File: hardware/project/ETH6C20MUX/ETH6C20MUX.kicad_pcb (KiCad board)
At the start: 4 copper layers, 160 x 100 mm, 184 parts, among them J301 5499141-4, J501 Conn_01x06, J502 Conn_02x08_Odd_Even, J503 C64AC, J601 Conn_02x05, J602 Conn_02x01, K301 HE3621A0510, K302 HE3621A0510, K303 HE3621A0510, K304 HE3621A0510, K305 HE3621A0510, K306 HE3621A0510, K307 HE3621A0510, K308 HE3621A0510, K309 HE3621A0510, K310 HE3621A0510, K311 HE3621A0510, K312 HE3621A0510, K313 HE3621A0510, K314 HE3621A0510, K315 HE3621A0510, K316 HE3621A0510, K317 HE3621A0510, K318 HE3621A0510, K319 HE3621A0510, K320 HE3621A0510, K321 HE3621A0510, K322 HE3621A0510, K323 HE3621A0510, K324 HE3621A0510, K325 HE3621A0510, K326 HE3621A0510, K327 HE3621A0510, K328 HE3621A0510, K329 HE3621A0510, K330 HE3621A0510, K331 HE3621A0510, K332 HE3621A0510, K333 HE3621A0510, K334 HE3621A0510, K335 HE3621A0510, K336 HE3621A0510, K337 HE3621A0510, K338 HE3621A0510, K339 HE3621A0510, K340 HE3621A0510, K341 HE3621A0510, K342 HE3621A0510, K343 HE3621A0510, K344 HE3621A0510, K345 HE3621A0510, K346 HE3621A0510, K347 HE3621A0510, K348 HE3621A0510, K349 HE3621A0510, K350 HE3621A0510, K351 HE3621A0510, K352 HE3621A0510, K353 HE3621A0510, K354 HE3621A0510, K355 HE3621A0510, K356 HE3621A0510, K357 HE3621A0510, K358 HE3621A0510, K359 HE3621A0510, K360 HE3621A0510, K361 HE3621A0510, K362 HE3621A0510, K363 HE3621A0510, K364 HE3621A0510, K365 HE3621A0510, K366 HE3621A0510, Q401 IRFR5410, U201 LC03-3.3, U202 LAN8742A, U203 LC03-3.3, U301 MCZ33996, U302 MCZ33996, U303 MCZ33996, U304 MCZ33996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

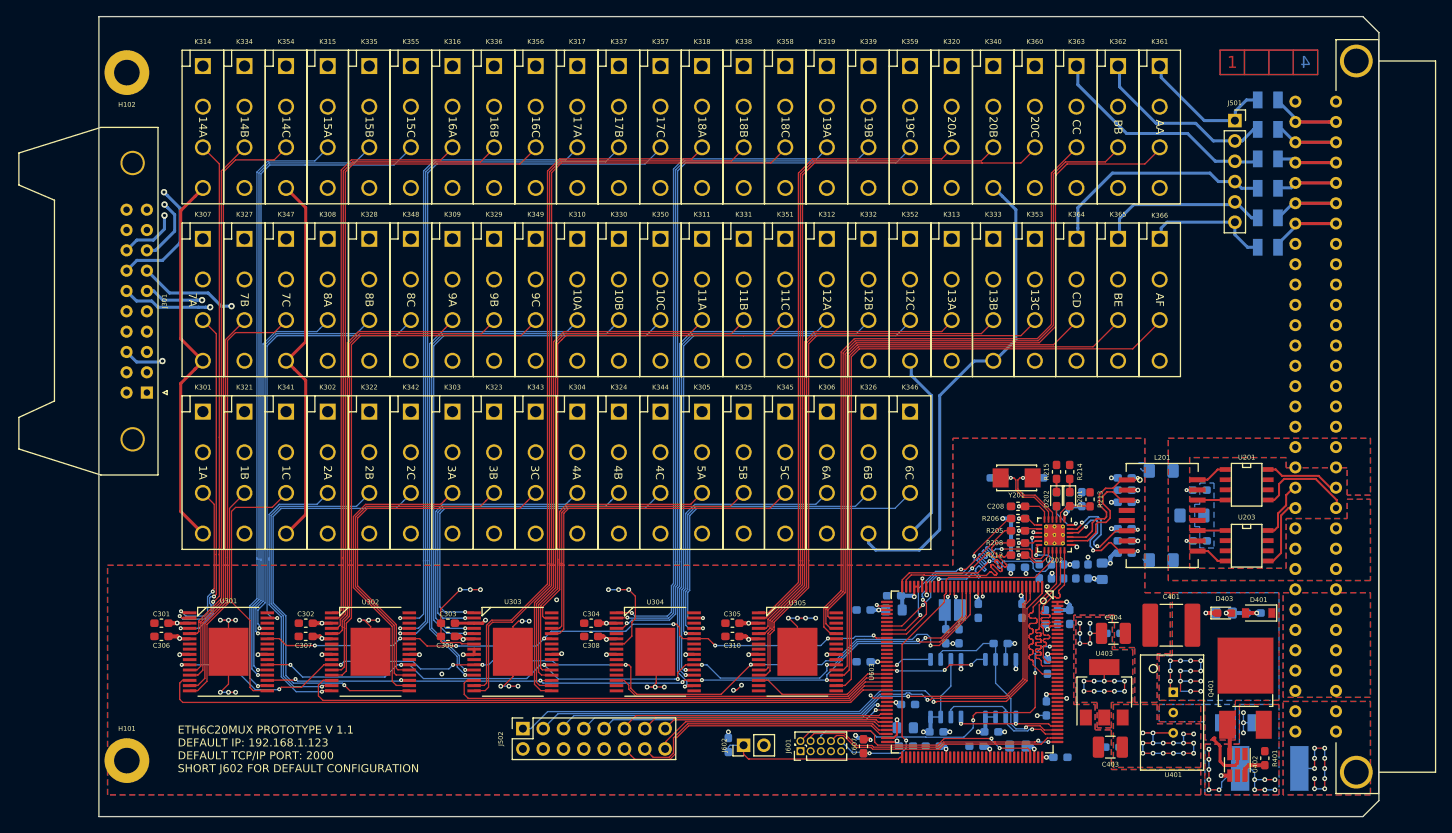
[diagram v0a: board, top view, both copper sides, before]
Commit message: Added pin swap for A,B,E and F.
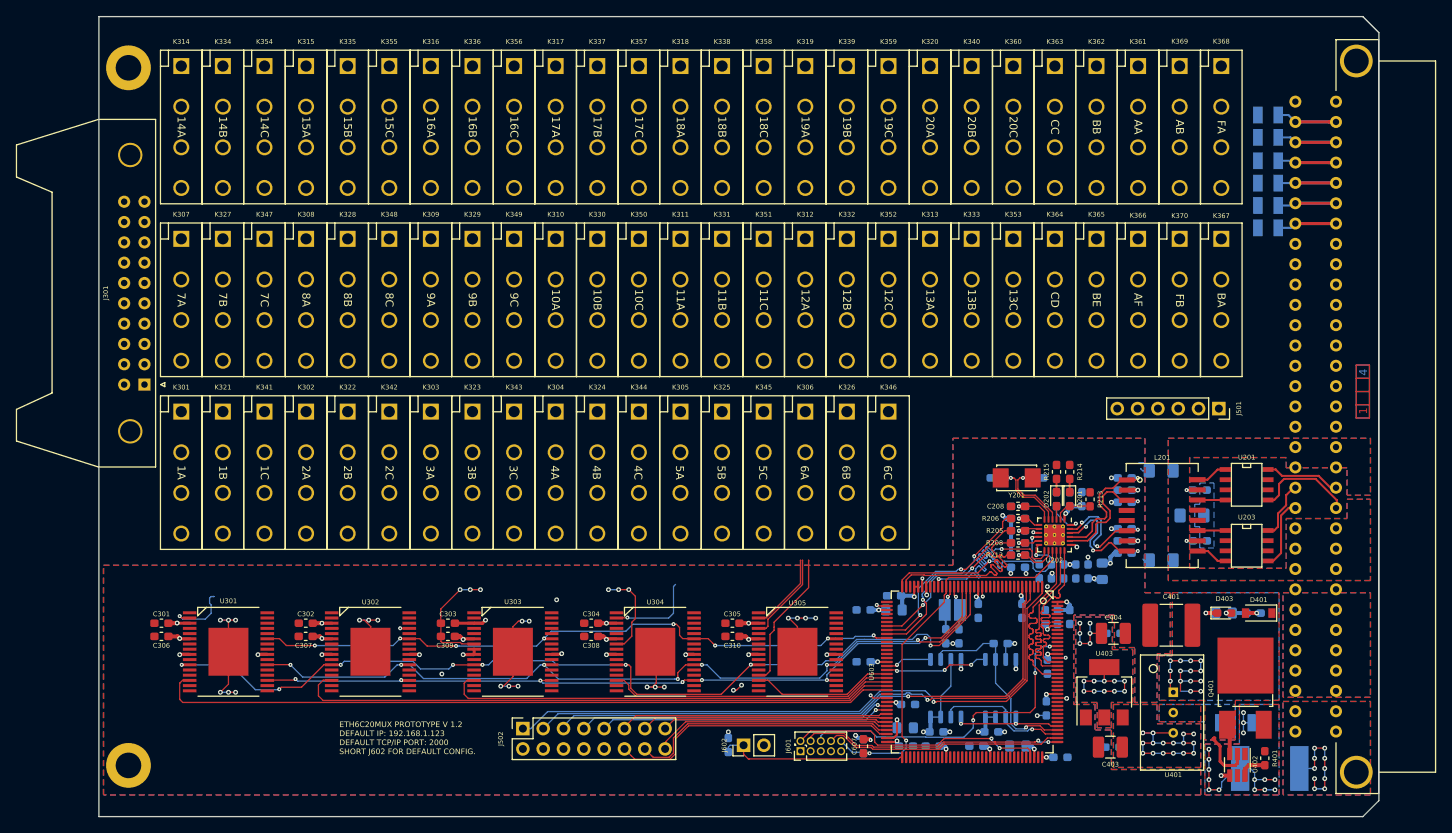
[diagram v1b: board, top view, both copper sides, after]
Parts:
- added K367: HE3621A0510, ETH6C20MUX:HE360_x-5050462-8, F.Cu at (200.3, 75.4)
- added K368: HE3621A0510, ETH6C20MUX:HE360_x-5050462-8, F.Cu at (200.3, 53.8)
- added K369: HE3621A0510, ETH6C20MUX:HE360_x-5050462-8, F.Cu at (195.1, 53.8)
- added K370: HE3621A0510, ETH6C20MUX:HE360_x-5050462-8, F.Cu at (195.1, 75.4)
- U601, U602: value S25FL064L_SOIC -> S25FL064L
- moved J501 36.1 mm to (200.0, 89.0), turned to 270 degrees
- moved K305 2.70 mm to (132.7, 97.0)
- moved K311 2.70 mm to (132.7, 75.4)
- moved K318 2.70 mm to (132.7, 53.8)
- moved K333 2.70 mm to (169.1, 75.4)
- moved K340 2.70 mm to (169.1, 53.8)
- moved K345 2.70 mm to (143.1, 97.0)
- moved K346 2.70 mm to (158.7, 97.0)
- moved K351 2.70 mm to (143.1, 75.4)
- moved K352 2.70 mm to (158.7, 75.4)
- moved K358 2.70 mm to (143.1, 53.8)
- moved K359 2.70 mm to (158.7, 53.8)
- moved K362 2.70 mm to (184.7, 53.8)
- moved K365 2.70 mm to (184.7, 75.4)
- moved K301 2.70 mm to (70.3, 97.0)
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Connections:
- U305 pad 15: (no net) -> /Relays/RELAYBA
- U305 pad 16: (no net) -> /Relays/RELAYEA
- U305 pad 17: (no net) -> /Relays/RELAYAB
- U305 pad 32: (no net) -> /Relays/RELAYFA
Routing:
- net /Relays/PIN10C: track 449.6 -> 0.00 mm
- net /Relays/PIN10B: track 435.5 -> 0.00 mm
- net /Relays/PIN10A: track 428.7 -> 0.00 mm
- net /Relays/PIN20: track 131.4 -> 0.00 mm
- net /Relays/PIN13: track 118.7 -> 0.00 mm, vias 1 -> 0
- net /Relays/PIN19: track 113.6 -> 0.00 mm
- net /Relays/PIN12: track 104.6 -> 0.00 mm, vias 1 -> 0
- net /Relays/PIN18: track 101.4 -> 0.00 mm
- net /Relays/PIN6: track 101.3 -> 0.00 mm, vias 1 -> 0
- net /Relays/RELAY18C: track 98.1 -> 0.00 mm
- net /Relays/RELAY18B: track 96.7 -> 0.00 mm
- net /Relays/RELAYA: track 96.0 -> 0.00 mm
- net /Relays/RELAY19C: track 94.1 -> 0.00 mm, vias 1 -> 0
- net /Relays/RELAYB: track 93.2 -> 0.66 mm
- net /Relays/RELAY17C: track 92.0 -> 0.00 mm, vias 1 -> 0
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- added copper zone on Power, net Earth
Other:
- board text added: "AB"
- board text added: "BA"
- board text added: "ETH6C20MUX PROTOTYPE V 1.2 DEFAULT IP: 192.168.1.123 DEFAULT TCP/IP PORT: 2000 SHORT J602 FOR DEFAULT CONFIG."
- board text added: "FA"
- board text added: "FB"
- board text removed: "ETH6C20MUX PROTOTYPE V 1.1 DEFAULT IP: 192.168.1.123 DEFAULT TCP/IP PORT: 2000 SHORT J602 FOR DEFAULT CONFIGURATION"

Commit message: PCB redesign
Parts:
- added D601: RED, LED_SMD:LED_0603_1608Metric_Pad1.05x0.95mm_HandSolder, F.Cu at (63.5, 113.7)
- added D602: GREEN, LED_SMD:LED_0603_1608Metric_Pad1.05x0.95mm_HandSolder, F.Cu at (63.5, 116.7)
- added D603: BLUE, LED_SMD:LED_0603_1608Metric_Pad1.05x0.95mm_HandSolder, F.Cu at (63.5, 119.5)
- added H103: MountingHole, MountingHole:MountingHole_2.7mm_M2.5_DIN965_Pad, F.Cu at (211.0, 46.0)
- added R602: 680, Resistor_SMD:R_0603_1608Metric_Pad0.98x0.95mm_HandSolder, F.Cu at (67.2, 113.7)
- added R603: 680, Resistor_SMD:R_0603_1608Metric_Pad0.98x0.95mm_HandSolder, F.Cu at (67.2, 116.7)
- added R605: 680, Resistor_SMD:R_0603_1608Metric_Pad0.98x0.95mm_HandSolder, F.Cu at (67.2, 119.5)
- added RN601: 10k, Resistor_SMD:R_Array_Convex_5x0603, B.Cu at (99.6, 131.3)
- added SW601: A6SN-5104, Button_Switch_SMD:SW_DIP_SPSTx05_Slide_6.7x14.26mm_W8.61mm_P2.54mm_LowProfile, F.Cu at (99.6, 131.3)
- C201, C202, C203, C204, C205, C206, C207, C208, C209, C210, C213, C214, C402, C405, C601, C602, C603, C604, C607, C608, C609, C610, C611, C612, C613, C614, C615, C616, C617, C618, C619, C620, C621: footprint Capacitor_SMD:C_0603_1608Metric_Pad1.05x0.95mm_HandSolder -> Capacitor_SMD:C_0603_1608Metric_Pad1.08x0.95mm_HandSolder
- C301, C302, C303, C304, C305, C306, C307, C308, C309, C310: footprint Capacitor_SMD:C_0603_1608Metric_Pad1.05x0.95mm_HandSolder -> Capacitor_SMD:C_0603_1608Metric_Pad1.08x0.95mm_HandSolder; moved to B.Cu
- D201: value YELLOW -> GREEN
- D202: value GREEN -> YELLOW
- H101, H102: footprint MountingHole:MountingHole_3.2mm_M3_DIN965_Pad -> MountingHole:MountingHole_2.7mm_M2.5_DIN965_Pad
- R201, R202, R203, R204, R205, R206, R207, R208, R209, R210, R211, R212, R213, R214, R215, R217, R218, R219, R220, R221, R401, R403, R601, R604, R608, R609: footprint Resistor_SMD:R_0603_1608Metric_Pad1.05x0.95mm_HandSolder -> Resistor_SMD:R_0603_1608Metric_Pad0.98x0.95mm_HandSolder
- R216: footprint Resistor_SMD:R_1206_3216Metric_Pad1.42x1.75mm_HandSolder -> Resistor_SMD:R_0603_1608Metric_Pad0.98x0.95mm_HandSolder
- R402: footprint Resistor_SMD:R_0805_2012Metric_Pad1.15x1.40mm_HandSolder -> Resistor_SMD:R_0603_1608Metric_Pad0.98x0.95mm_HandSolder
- moved K360 93.6 mm to (80.7, 53.8)
- moved K320 93.6 mm to (70.3, 53.8)
- moved K340 93.6 mm to (75.5, 53.8)
- moved K334 93.5 mm to (169.0, 53.8)
- moved K314 93.5 mm to (163.8, 53.8)
- moved K354 93.5 mm to (174.2, 53.8)
- moved K319 62.4 mm to (85.9, 53.8)
- moved K339 62.4 mm to (91.1, 53.8)
- moved K359 62.4 mm to (96.3, 53.8)
- moved K355 62.4 mm to (158.7, 53.8)
- moved K315 62.4 mm to (148.3, 53.8)
- moved K335 62.4 mm to (153.5, 53.8)
- moved K338 31.2 mm to (106.7, 53.8)
- moved K318 31.2 mm to (101.5, 53.8)
- moved K358 31.2 mm to (111.9, 53.8)
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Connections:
- J501 pad 4: /Connector/D -> /Connector/F
- J501 pad 6: /Connector/F -> /Connector/D
- U301 pad 12: /Relays/RELAY14C -> /Relays/RELAY7B
- U301 pad 13: /Relays/RELAY7B -> /Relays/RELAY1B
- U301 pad 15: /Relays/RELAY7C -> /Relays/RELAY14C
- U301 pad 16: /Relays/RELAY1B -> /Relays/RELAY8C
- U301 pad 17: /Relays/RELAY1C -> /Relays/RELAY8B
- U301 pad 29: /Relays/RELAY8B -> (no net)
- U301 pad 31: /Relays/RELAY8C -> /Relays/RELAY7C
- U301 pad 32: (no net) -> /Relays/RELAY1C
- U301 pad 4: /Relays/RELAY14A -> /Relays/RELAY20A
- U301 pad 5: /Relays/RELAY14B -> /Relays/RELAY20B
- U305 pad 1: /Relays/RELAY20A -> /Relays/RELAY14A
- U305 pad 2: /Relays/RELAY20B -> /Relays/RELAY14B
- U603 pad 74: (no net) -> /MCU/ETH_CODE4
- U603 pad 75: (no net) -> /MCU/ETH_CODE3
- U603 pad 76: (no net) -> /MCU/ETH_CODE2
- U603 pad 77: (no net) -> /MCU/ETH_CODE1
- U603 pad 78: (no net) -> /MCU/ETH_CODE0
- U603 pad 80: (no net) -> Net-(R602-Pad2)
- U603 pad 81: (no net) -> Net-(R603-Pad2)
- U603 pad 82: (no net) -> Net-(R605-Pad2)
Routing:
- net /Relays/PIN10B: track 0.00 -> 446.1 mm
- net /Relays/PIN10A: track 0.00 -> 445.9 mm
- net /Relays/PIN10C: track 0.00 -> 366.8 mm
- net /Relays/PIN14: track 0.00 -> 132.0 mm
- net /Connector/C: track 0.00 -> 117.3 mm
- net /MCU/RELAY1_SCLK: track 118.0 -> 0.77 mm, vias 8 -> 0
- net /Relays/PIN13: track 0.00 -> 114.3 mm
- net Net-(R602-Pad2): track 0.00 -> 112.7 mm
- net Net-(R603-Pad2): track 0.00 -> 110.6 mm
- net /Relays/PIN15: track 0.00 -> 110.0 mm
- net Net-(R605-Pad2): track 0.00 -> 108.8 mm
- net /Relays/PIN6: track 0.00 -> 102.6 mm
- net /Relays/PIN12: track 0.00 -> 102.2 mm
- net /MCU/RELAY1_SO: track 103.7 -> 2.10 mm, vias 7 -> 1
- net /MCU/RELAY1_SI: track 98.6 -> 0.00 mm, vias 7 -> 0
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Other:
- net class Relay signal 100V: trace_width 0.381 -> 0.254
- board text added: "EA"
- board text removed: "FA"

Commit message: PCB design
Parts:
- D601, D602, D603: footprint LED_SMD:LED_0603_1608Metric_Pad1.05x0.95mm_HandSolder -> LED_SMD:LED_Dialight_591
- J501: value Conn_01x06 -> Conn_02x06_Odd_Even; footprint Connector_PinSocket_2.54mm:PinSocket_1x06_P2.54mm_Vertical -> Connector_PinSocket_2.54mm:PinSocket_2x06_P2.54mm_Vertical
- R216: footprint Resistor_SMD:R_0603_1608Metric_Pad0.98x0.95mm_HandSolder -> Resistor_SMD:R_1206_3216Metric_Pad1.30x1.75mm_HandSolder
- moved J501 11.2 mm to (189.0, 91.0)
- moved R605 6.16 mm to (68.7, 125.5)
- moved D603 5.98 mm to (63.1, 125.5)
- moved R603 3.41 mm to (68.7, 119.8)
- moved D602 3.07 mm to (63.1, 119.8)
- moved R602 1.57 mm to (68.7, 114.0)
- moved C212 1.09 mm to (192.4, 109.0)
- moved D601 0.54 mm to (63.1, 114.0)
- moved R216 0.54 mm to (192.4, 96.4)
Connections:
- J501 pad 2: /Connector/B -> /Connector/A
- J501 pad 3: /Connector/C -> /Connector/B
- J501 pad 4: /Connector/F -> /Connector/B
- J501 pad 5: /Connector/E -> /Connector/C
- J501 pad 6: /Connector/D -> /Connector/C
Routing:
- net /Connector/C: track 117.3 -> 35.0 mm
- net /Connector/A: track 75.7 -> 25.0 mm
- net /Connector/D: track 58.6 -> 32.4 mm
- net /Connector/B: track 72.1 -> 46.3 mm
- net /Connector/F: track 39.8 -> 16.1 mm
- net /Connector/E: track 66.3 -> 43.0 mm
- net +3V3: track 150.2 -> 128.8 mm, vias 44 -> 43
- net GND: track 42.4 -> 32.3 mm, vias 31 -> 28
- net Net-(R605-Pad2): track 108.8 -> 102.5 mm
- net Net-(R603-Pad2): track 110.6 -> 106.2 mm
- net Net-(R602-Pad2): track 112.7 -> 110.8 mm
- net Net-(D603-Pad1): track 1.90 -> 3.08 mm
- net Net-(D602-Pad1): track 1.90 -> 3.08 mm
- net Net-(D601-Pad1): track 1.90 -> 3.08 mm
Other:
- board text added: "ETH6C20MUX PROTOTYPE V 1.1 DEFAULT IP: 192.168.1.120 DEFAULT TCP/IP PORT: 2000 SHORT J602 FOR DEFAULT CONFIG."
- board text removed: "ETH6C20MUX PROTOTYPE V 1.2 DEFAULT IP: 192.168.1.123 DEFAULT TCP/IP PORT: 2000 SHORT J602 FOR DEFAULT CONFIG."

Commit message: PCB layout
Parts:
- moved C301 1.69 mm to (73.2, 113.4)
- moved U305 1.67 mm to (147.0, 117.0)
- moved C302 1.67 mm to (89.7, 113.4)
- moved C303 1.66 mm to (106.2, 113.4)
- moved C304 1.65 mm to (122.7, 113.4)
- moved C305 1.65 mm to (139.2, 113.4)
- moved U304 1.65 mm to (130.5, 117.0)
- moved U303 1.65 mm to (114.0, 117.0)
- moved U301 1.64 mm to (81.0, 117.0)
- moved U302 1.64 mm to (97.5, 117.0)
- moved C308 1.52 mm to (122.7, 115.4)
- moved C306 1.33 mm to (73.2, 115.4)
- moved C307 1.30 mm to (89.7, 115.4)
- moved C309 1.28 mm to (106.2, 115.4)
- moved C310 1.27 mm to (139.2, 115.4)
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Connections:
- K315 pad 3: /Relays/RELAY15A -> (no net)
- K335 pad 3: /Relays/RELAY15B -> (no net)
- K354 pad 3: /Relays/RELAY14C -> (no net)
- K355 pad 3: /Relays/RELAY15C -> (no net)
- U301 pad 1: /Relays/RELAY1A -> /Relays/RELAY20C
- U301 pad 12: /Relays/RELAY7B -> /Relays/RELAY20B
- U301 pad 13: /Relays/RELAY1B -> /Relays/RELAY20A
- U301 pad 15: /Relays/RELAY14C -> /Relays/RELAY7A
- U301 pad 16: /Relays/RELAY8C -> /Relays/RELAY1A
- U301 pad 17: /Relays/RELAY8B -> /Relays/RELAY1C
- U301 pad 18: /Relays/RELAY15A -> /Relays/RELAY19A
- U301 pad 2: /Relays/RELAY7A -> /Relays/RELAY7C
- U301 pad 20: /Relays/RELAY15B -> /Relays/RELAY8A
- U301 pad 21: /Relays/RELAY15C -> /Relays/RELAY2A
- U301 pad 28: /Relays/RELAY8A -> (no net)
- U301 pad 29: (no net) -> /Relays/RELAY2B
- U301 pad 31: /Relays/RELAY7C -> /Relays/RELAY8B
- U301 pad 32: /Relays/RELAY1C -> /Relays/RELAY19B
- U301 pad 4: /Relays/RELAY20A -> /Relays/RELAY1B
- U301 pad 5: /Relays/RELAY20B -> /Relays/RELAY7B
- U302 pad 1: /Relays/RELAY16A -> /Relays/RELAY9B
- U302 pad 12: /Relays/RELAY9B -> /Relays/RELAY18A
- U302 pad 13: /Relays/RELAY9C -> /Relays/RELAY2C
- U302 pad 15: /Relays/RELAY2B -> /Relays/RELAY8C
- U302 pad 16: /Relays/RELAY2A -> /Relays/RELAY19C
- U302 pad 17: /Relays/RELAY2C -> /Relays/RELAY3B
- U302 pad 18: /Relays/RELAY3A -> /Relays/RELAY18C
- U302 pad 2: /Relays/RELAY16B -> /Relays/RELAY18B
- U302 pad 20: /Relays/RELAY3B -> /Relays/RELAY9C
- U302 pad 28: /Relays/RELAY17C -> /Relays/RELAY4A
- U302 pad 29: /Relays/RELAY17B -> /Relays/RELAY10A
- U302 pad 4: /Relays/RELAY16C -> /Relays/RELAY3A
- U303 pad 1: /Relays/RELAY4C -> /Relays/RELAY11A
- U303 pad 12: /Relays/RELAY10B -> /Relays/RELAY17C
- U303 pad 13: /Relays/RELAY10A -> /Relays/RELAY4B
- U303 pad 15: /Relays/RELAY18A -> /Relays/RELAY10B
- U303 pad 16: /Relays/RELAY18B -> /Relays/RELAY17B
- U303 pad 17: /Relays/RELAY18C -> /Relays/RELAY5A
- U303 pad 18: /Relays/RELAY11A -> /Relays/RELAY16B
- U303 pad 2: /Relays/RELAY4B -> /Relays/RELAY16A
- U303 pad 21: /Relays/RELAY11C -> /Relays/RELAY5B
- U303 pad 29: /Relays/RELAY5B -> /Relays/RELAY11C
- U303 pad 31: /Relays/RELAY5A -> /Relays/RELAY16C
- U303 pad 4: /Relays/RELAY4A -> /Relays/RELAY4C
- U304 pad 1: /Relays/RELAY19A -> (no net)
- U304 pad 2: /Relays/RELAY19B -> (no net)
- U304 pad 4: /Relays/RELAY19C -> (no net)
- U305 pad 4: /Relays/RELAY20C -> (no net)
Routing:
- net /MCU/RELAY1_SCLK: track 0.77 -> 104.8 mm, vias 0 -> 6
- net /MCU/RELAY1_SI: track 0.00 -> 97.3 mm, vias 0 -> 6
- net /MCU/RELAY1_SO: track 2.10 -> 95.1 mm, vias 1 -> 7
- net /MCU/RELAY1_~CS0: track 0.00 -> 83.8 mm
- net /Relays/RELAY16B: track 0.00 -> 83.5 mm
- net /MCU/RELAY1_~RST: track 0.00 -> 82.4 mm, vias 0 -> 5
- net /Relays/RELAY17C: track 0.00 -> 80.1 mm
- net /Relays/RELAY16C: track 0.00 -> 78.5 mm
- net /Relays/RELAY17B: track 1.17 -> 79.2 mm, vias 1 -> 0
- net /Relays/RELAY16A: track 0.00 -> 77.0 mm
- net /Relays/RELAY18C: track 0.00 -> 74.5 mm
- net /Relays/RELAY18A: track 0.00 -> 73.2 mm
- net /Relays/RELAY19C: track 0.00 -> 70.4 mm
- net /Relays/RELAY18B: track 0.00 -> 69.9 mm
- net /Relays/RELAY19A: track 0.00 -> 68.0 mm
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
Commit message: PCB layout
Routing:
- net /Connector/C: track 35.0 -> 95.2 mm, vias 0 -> 1
- net /Connector/A: track 25.0 -> 77.6 mm, vias 0 -> 1
- net /Connector/B: track 46.3 -> 79.2 mm
- net /Connector/F: track 16.1 -> 43.9 mm
- net /Connector/D: track 32.4 -> 60.0 mm
- net /Connector/E: track 43.0 -> 69.7 mm
- net GND: track 25.0 -> 36.5 mm, vias 22 -> 74
- net /MCU/RELAY1_SCLK: track 104.8 -> 109.2 mm
- net /MCU/RELAY1_~RST: track 82.4 -> 84.5 mm
